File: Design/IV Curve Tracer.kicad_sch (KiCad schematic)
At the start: 10 parts, among them J101 9V Supply, SW101 SW_Push, U101 MCU_Nucleo_L432KC

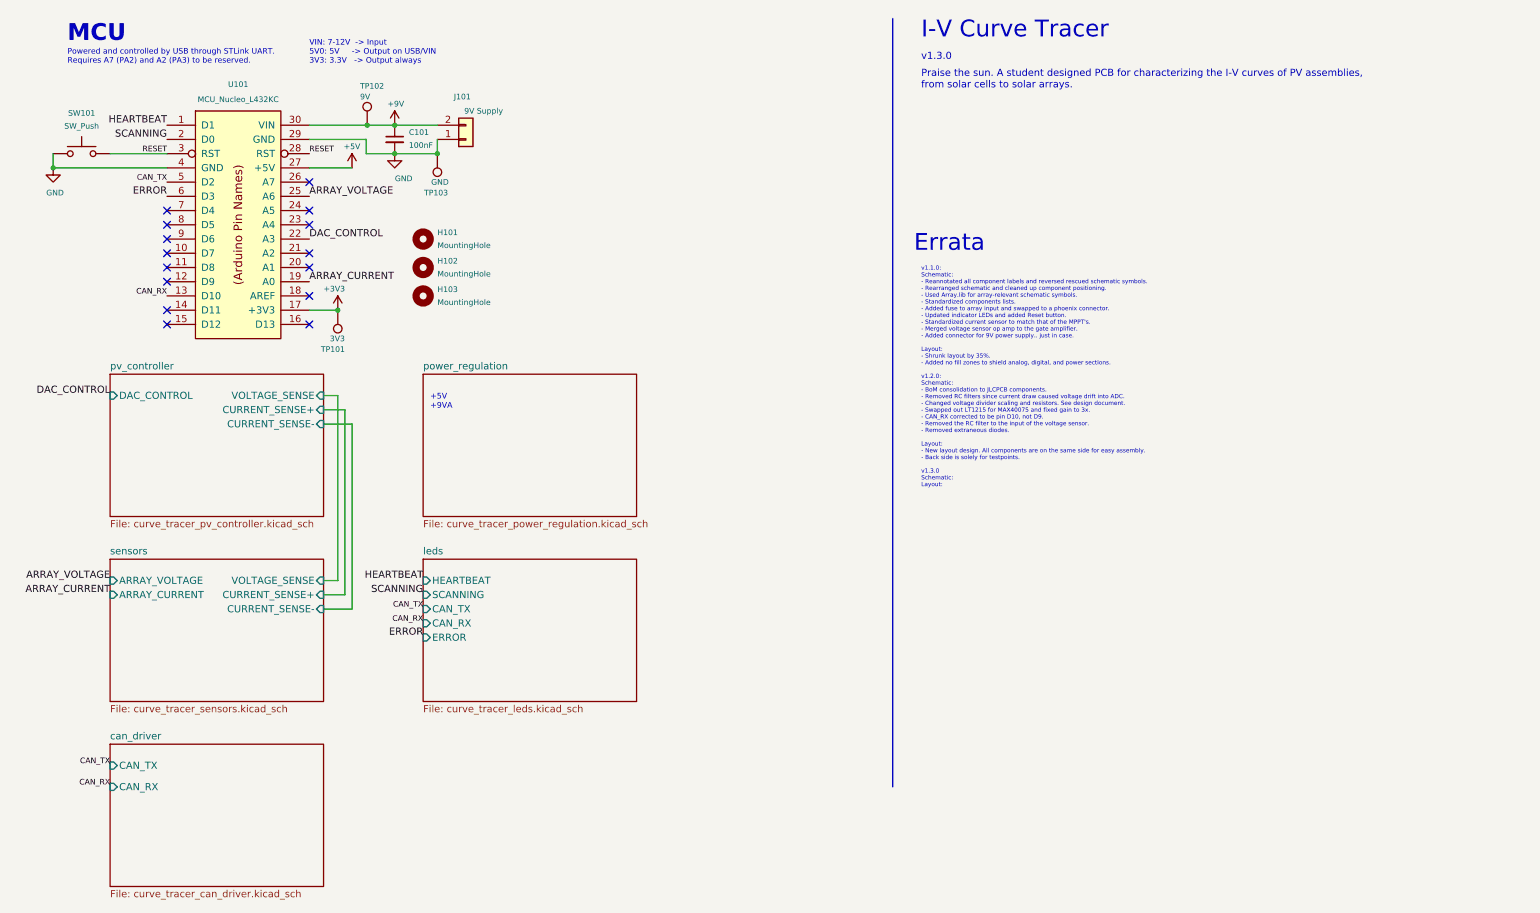
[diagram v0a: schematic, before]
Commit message: cleanup and fix errors for v1.3.0, proposed v1.4.0
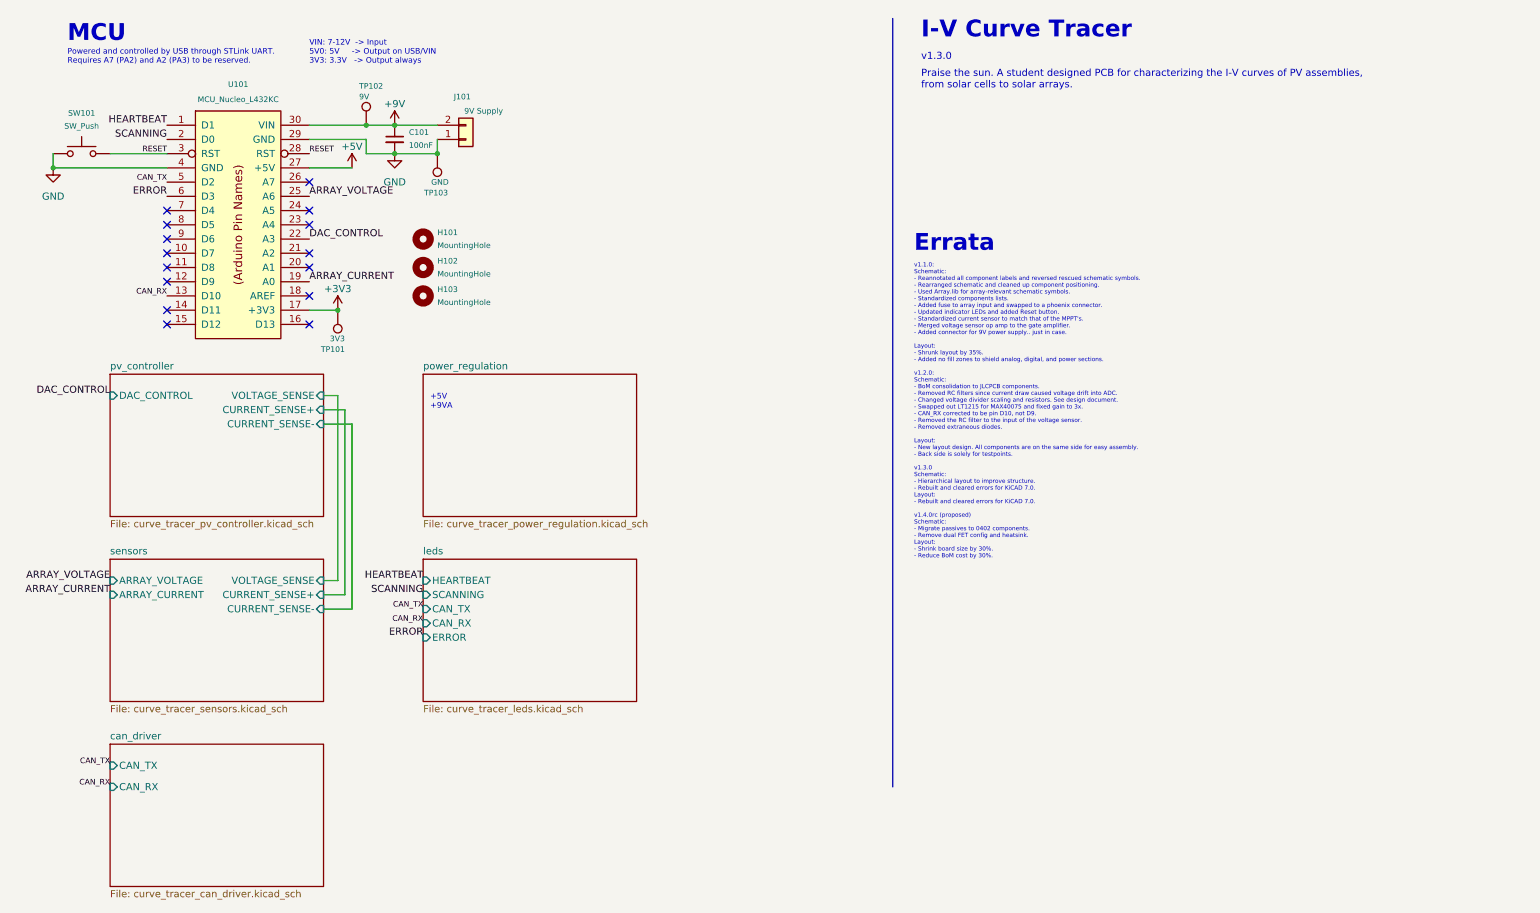
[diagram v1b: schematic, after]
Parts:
- C101: Cost (none) -> 0.0078; JLCPCB BOM 1 -> (none); LCSC Part C28233 -> (none); LCSC Part # (none) -> C28233; P/N (none) -> CL21B104KCFNNNE; Part Number N/A -> (none); Projected Cost 0.0083 -> (none); Purchase Page N/A -> (none)
- H101, H102, H103, TP101, TP102, TP103: Part Number N/A -> (none)
- J101: Cost (none) -> 0.97; JLCPCB BOM 0 -> (none); LCSC Part N/A -> (none); P/N (none) -> 43650-0215; Part Number 538-43650-0215 -> (none); Projected Cost 1.46 -> (none); Purchase Page https://www.mouser.com/ProductDetail/538-43650-0215 -> (none)
- SW101: Cost (none) -> 0.10; JLCPCB BOM 0 -> (none); LCSC Part N/A -> (none); P/N (none) -> TS02-66-50-BK-260-SCR-D; Part Number 179-TS026650BK260SCR -> (none); Projected Cost 0.10 -> (none); Purchase Page https://www.mouser.com/ProductDetail/CUI-Devices/TS02-66-50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 -> (none)
- U101: Cost (none) -> 10.99; JLCPCB BOM 0 -> (none); LCSC Part N/A -> (none); P/N (none) -> NUCLEO-L432KC; Part Number 511-NUCLEO-L432KC -> (none); Projected Cost 10.64 -> (none); Purchase Page https://www.mouser.com/ProductDetail/STMicroelectronics/NUC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 -> (none)
